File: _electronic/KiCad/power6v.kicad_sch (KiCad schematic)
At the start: 14 parts

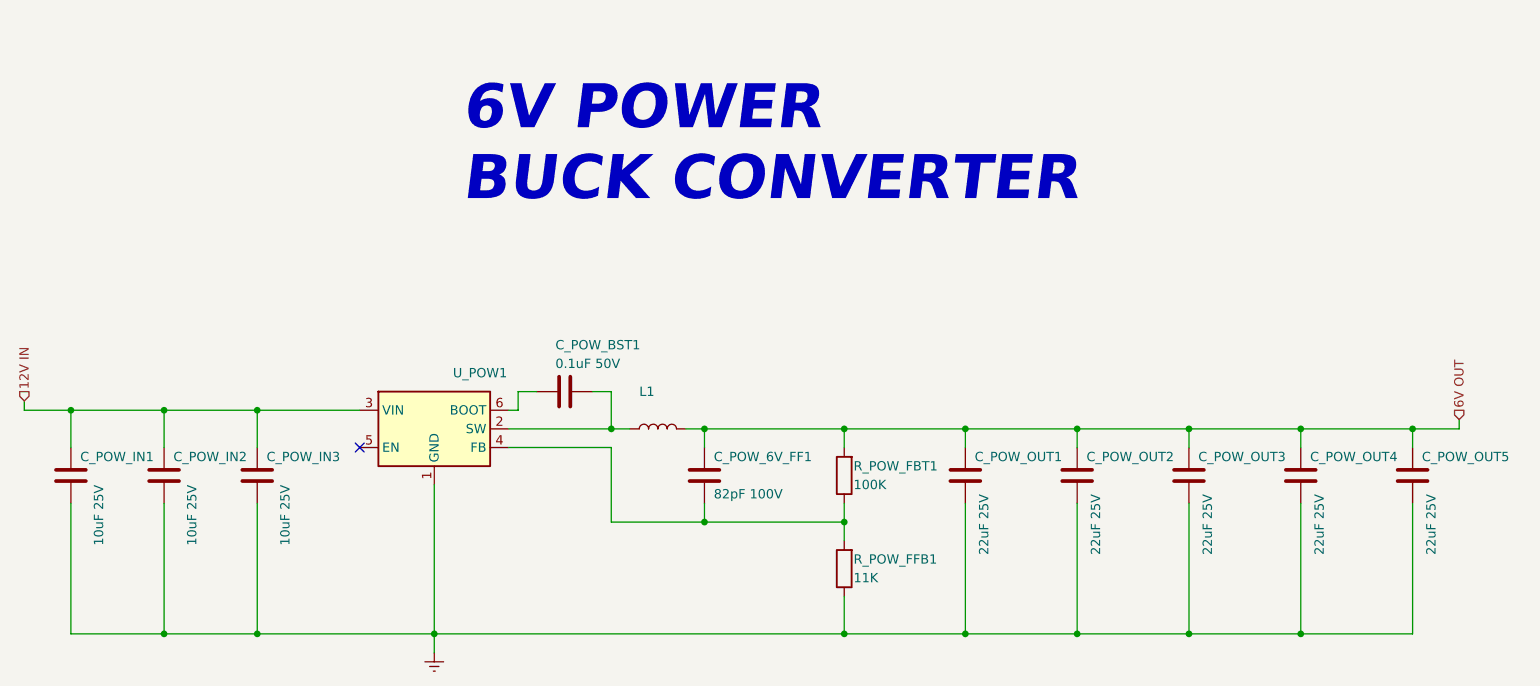
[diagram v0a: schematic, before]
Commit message: 6v and power latch backup
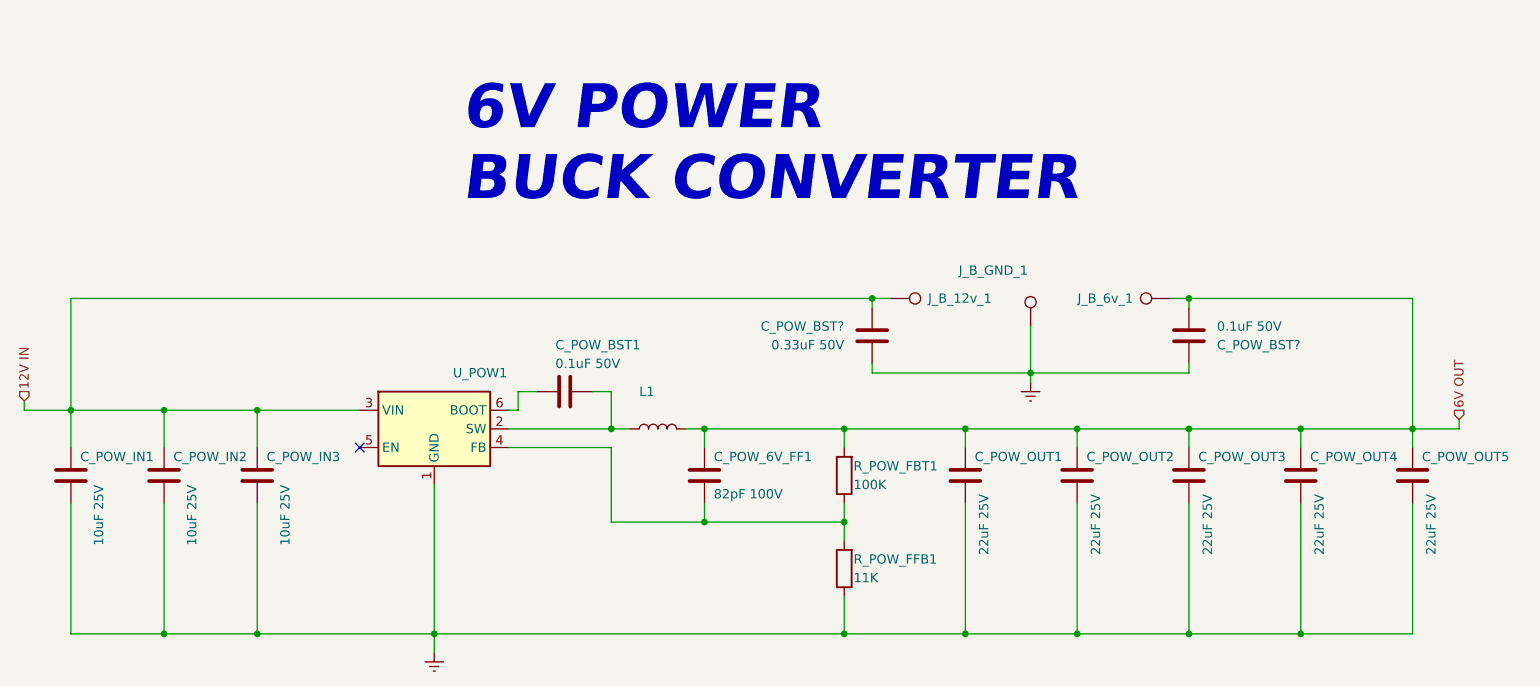
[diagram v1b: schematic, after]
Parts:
- added C_POW_BST?: 0.1uF 50V, Capacitor_SMD:C_0603_1608Metric_Pad1.08x0.95mm_HandSolder, symbol Device:C
- added C_POW_BST?: 0.33uF 50V, Capacitor_SMD:C_0603_1608Metric_Pad1.08x0.95mm_HandSolder, symbol Device:C
- added J_B_12v_1, J_B_6v_1, J_B_GND_1: TestPoint, TestPoint:TestPoint_Pad_D1.5mm, symbol Connector:TestPoint
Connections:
- net 12V IN: now also C_POW_BST?.2, J_B_12v_1.1
- net 6V OUT: now also C_POW_BST?.1, J_B_6v_1.1
- net GNDREF: now also C_POW_BST?.1, C_POW_BST?.2, J_B_GND_1.1

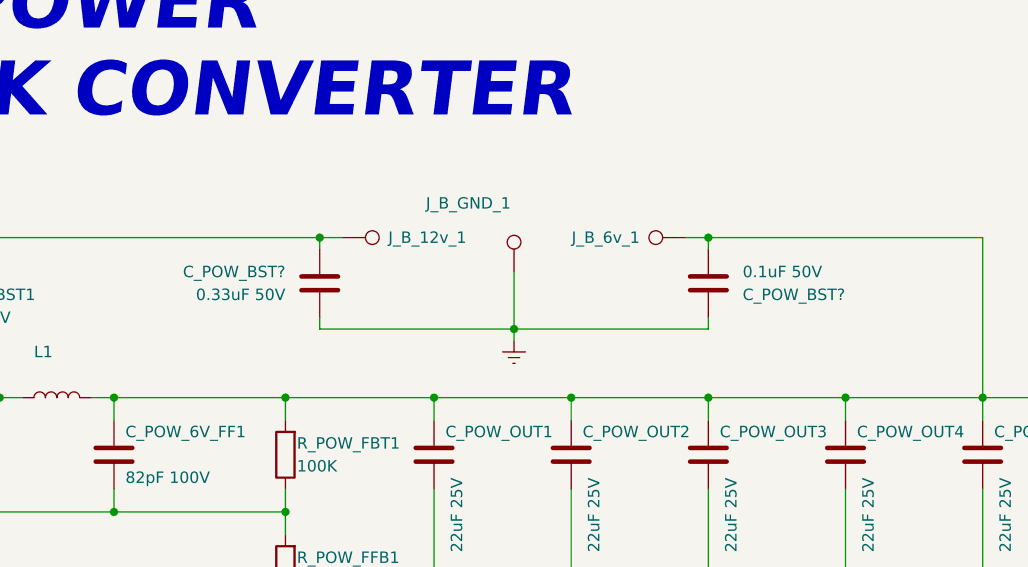
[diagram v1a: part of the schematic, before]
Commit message: uln2003 soic narrow
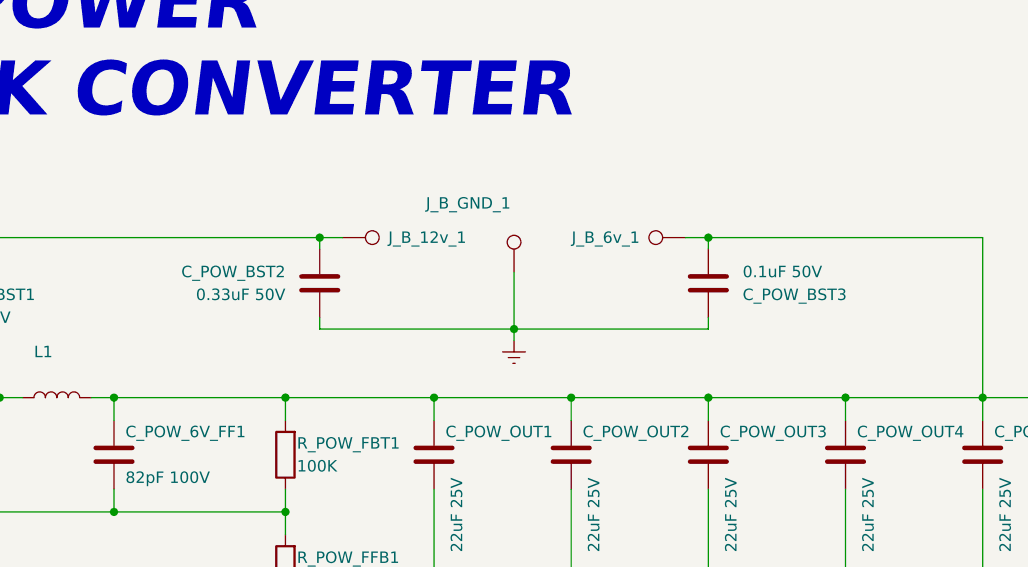
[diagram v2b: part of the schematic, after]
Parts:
- gave numbers to parts that had none: 2
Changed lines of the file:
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@@
   (symbol (lib_id "Device:C") (at 210.82 78.74 0) (unit 1)
     (in_bom yes) (on_board yes)
-    (property "Reference" "C_POW_BST?" (id 0) (at 214.63 80.01 0)
+    (property "Reference" "C_POW_BST3" (id 0) (at 214.63 80.01 0)
       (effects (font (size 1.27 1.27)) (justify left))
     )
@@
   (symbol (lib_id "Device:C") (at 167.64 78.74 180) (unit 1)
     (in_bom yes) (on_board yes)
-    (property "Reference" "C_POW_BST?" (id 0) (at 163.83 77.47 0)
+    (property "Reference" "C_POW_BST2" (id 0) (at 163.83 77.47 0)
       (effects (font (size 1.27 1.27)) (justify left))
     )

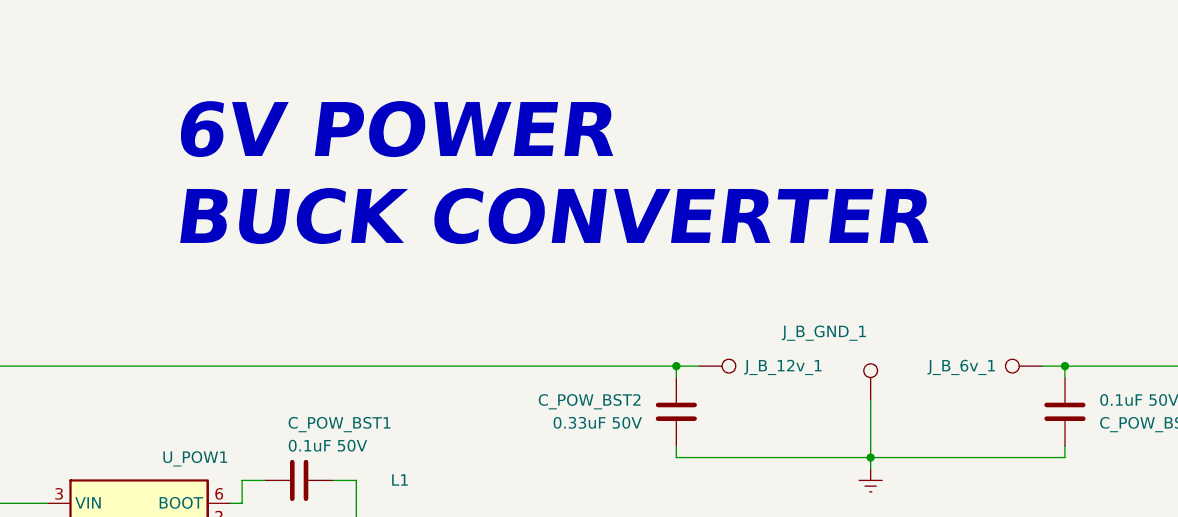
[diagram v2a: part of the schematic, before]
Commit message: revised IC packages, pins and footprints
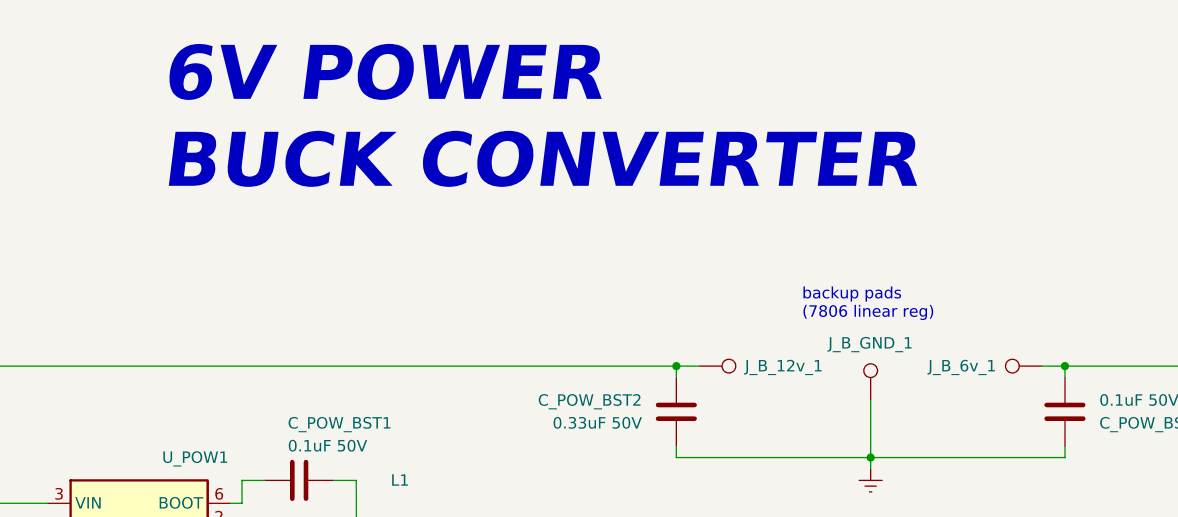
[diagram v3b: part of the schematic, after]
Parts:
- U_POW1: footprint Package_TO_SOT_SMD:SOT-23-6 -> Package_TO_SOT_SMD:SOT-23-6_Handsoldering
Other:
- note added: "backup pads (7806 linear reg)"
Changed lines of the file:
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@@
     (stroke (width 0) (type default) (color 0 0 0 0))
   )
-  (text "6V POWER\nBUCK CONVERTER" (at 111.76 60.96 0)
+  (text "backup pads\n(7806 linear reg)" (at 181.61 68.58 0)
+    (effects (font (size 1.27 1.27)) (justify left bottom))
+  )
+  (text "6V POWER\nBUCK CONVERTER" (at 110.49 54.61 0)
     (effects (font (size 6 6) (thickness 0.6) bold italic) (justify left bottom))
   )
@@
   (symbol (lib_id "Connector:TestPoint") (at 189.23 77.47 0) (unit 1)
     (in_bom yes) (on_board yes)
-    (property "Reference" "J_B_GND_1" (id 0) (at 184.15 69.85 0))
+    (property "Reference" "J_B_GND_1" (id 0) (at 189.23 71.12 0))
     (property "Value" "TestPoint" (id 1) (at 189.23 72.39 90)
       (effects (font (size 1.27 1.27)) (justify left) hide)
@@
       (effects (font (size 1.27 1.27)) (justify left))
     )
-    (property "Footprint" "Package_TO_SOT_SMD:SOT-23-6" (id 2) (at 109.22 100.33 0)
+    (property "Footprint" "Package_TO_SOT_SMD:SOT-23-6_Handsoldering" (id 2) (at 109.22 100.33 0)
       (effects (font (size 1.27 1.27)) (justify left) hide)
     )

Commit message: schematics footer and export
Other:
- company: (none) -> Andrei Speridiao
- title: (none) -> E-TKT
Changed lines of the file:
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@@
 (kicad_sch (version 20211123) (generator eeschema)
   (paper "A4")
+  (title_block
+    (title "E-TKT")
+    (date "2022-07-21")
+    (rev "3")
+    (company "Andrei Speridiao")
+  )
   (junction (at 195.58 119.38) (diameter 0) (color 0 0 0 0)
   )
